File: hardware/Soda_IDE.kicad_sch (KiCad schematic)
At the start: 25 parts, among them CN1 MSX_SLOT_CON, J2 Conn_CF_Card, J3 Conn_02x22_Odd_Even, Q1 BC548, SW1 SW_Push, SW2 SW_Push_SPDT, U1 27C512, U2 74HCT74, U3 74LS32, U4 74HCT138

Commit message: fixes and updates
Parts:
- added JP2, JP3, JP4: SolderJumper_2_Open, Jumper:SolderJumper-2_P1.3mm_Open_RoundedPad1.0x1.5mm, symbol Jumper:SolderJumper_2_Open
- U2: renamed from U3; value 74LS32 -> 74HCT32
- renumbered C3 to C2, C2 to C3, D2 to D1, J3 to J1, JP2 to J2, J2 to J3, D1 to LD1, R6 to R1, R4 to R2, R5 to R3, R2 to R4, R1 to R5, R3 to R6, U2 to U3
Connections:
- net IORQ is gone; now on net ~{IORQ}: U3.13 (~{R})
- net ~{SEL} is gone; now on net ~{IDE_CS0}: J3.7 (Pin_7)
- net ~{IDE_CS0}: now also JP2.2 (B), JP3.2 (B), JP4.2 (B); no longer U4.13 (~{Y2})
- net at U4.12 (~{Y3}): now also JP2.1 (A)
- net at U4.15 (~{Y0}): now also JP4.1 (A)
- new net: JP3.1 (A), U4.13 (~{Y2})
- no-connect marks 62 -> 58
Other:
- note added: "JP2: 38h..3fh"
- note added: "JP3: 30h..37h"
- note added: "JP4 10h..17h"
- note added: "Z80 Reset (Optional)"
- note removed: "0011 0XXX"
- note removed: "30h..37h"
- moved on the sheet: C2, C3, CN1, SW2, U3B, U4

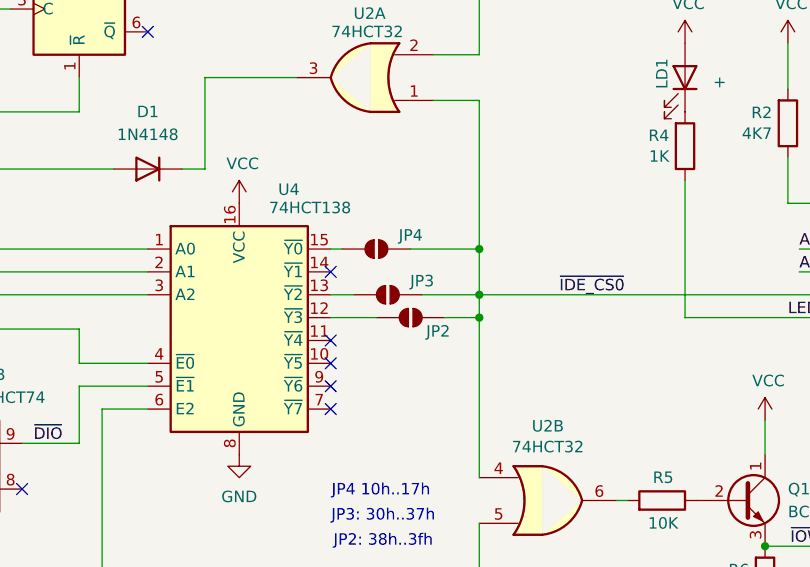
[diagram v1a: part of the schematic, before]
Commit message: conventional jumpers for address selection
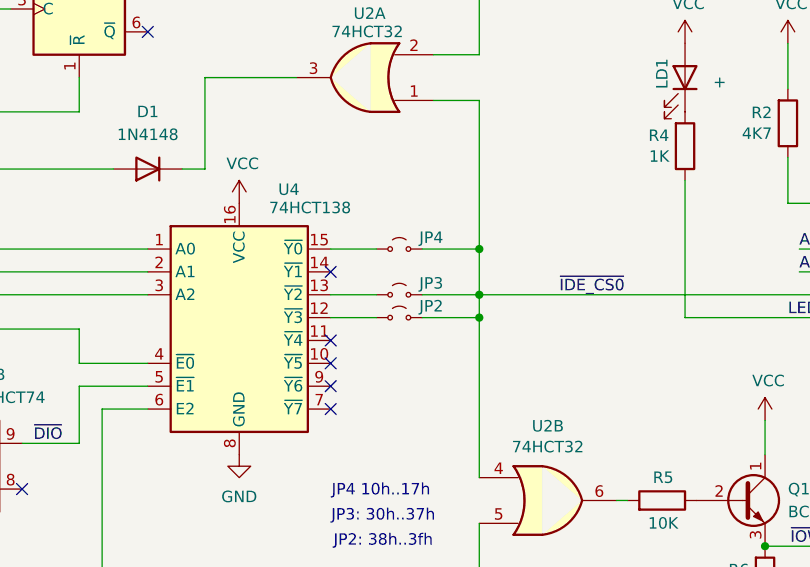
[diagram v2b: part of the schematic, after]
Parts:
- removed JP2, JP3, JP4: SolderJumper_2_Open, Jumper:SolderJumper-2_P1.3mm_Open_RoundedPad1.0x1.5mm, symbol Jumper:SolderJumper_2_Open
- added JP2, JP3, JP4: Jumper_2_Small_Open, Connector_PinHeader_2.54mm:PinHeader_1x02_P2.54mm_Vertical, symbol Jumper:Jumper_2_Small_Open
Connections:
- net ~{IDE_CS0}: now also JP2.2 (B), JP3.2 (B), JP4.2 (B)
- net at U4.15 (~{Y0}): now also JP4.1 (A)
- net at U4.12 (~{Y3}): now also JP2.1 (A)
- net at U4.13 (~{Y2}): now also JP3.1 (A)

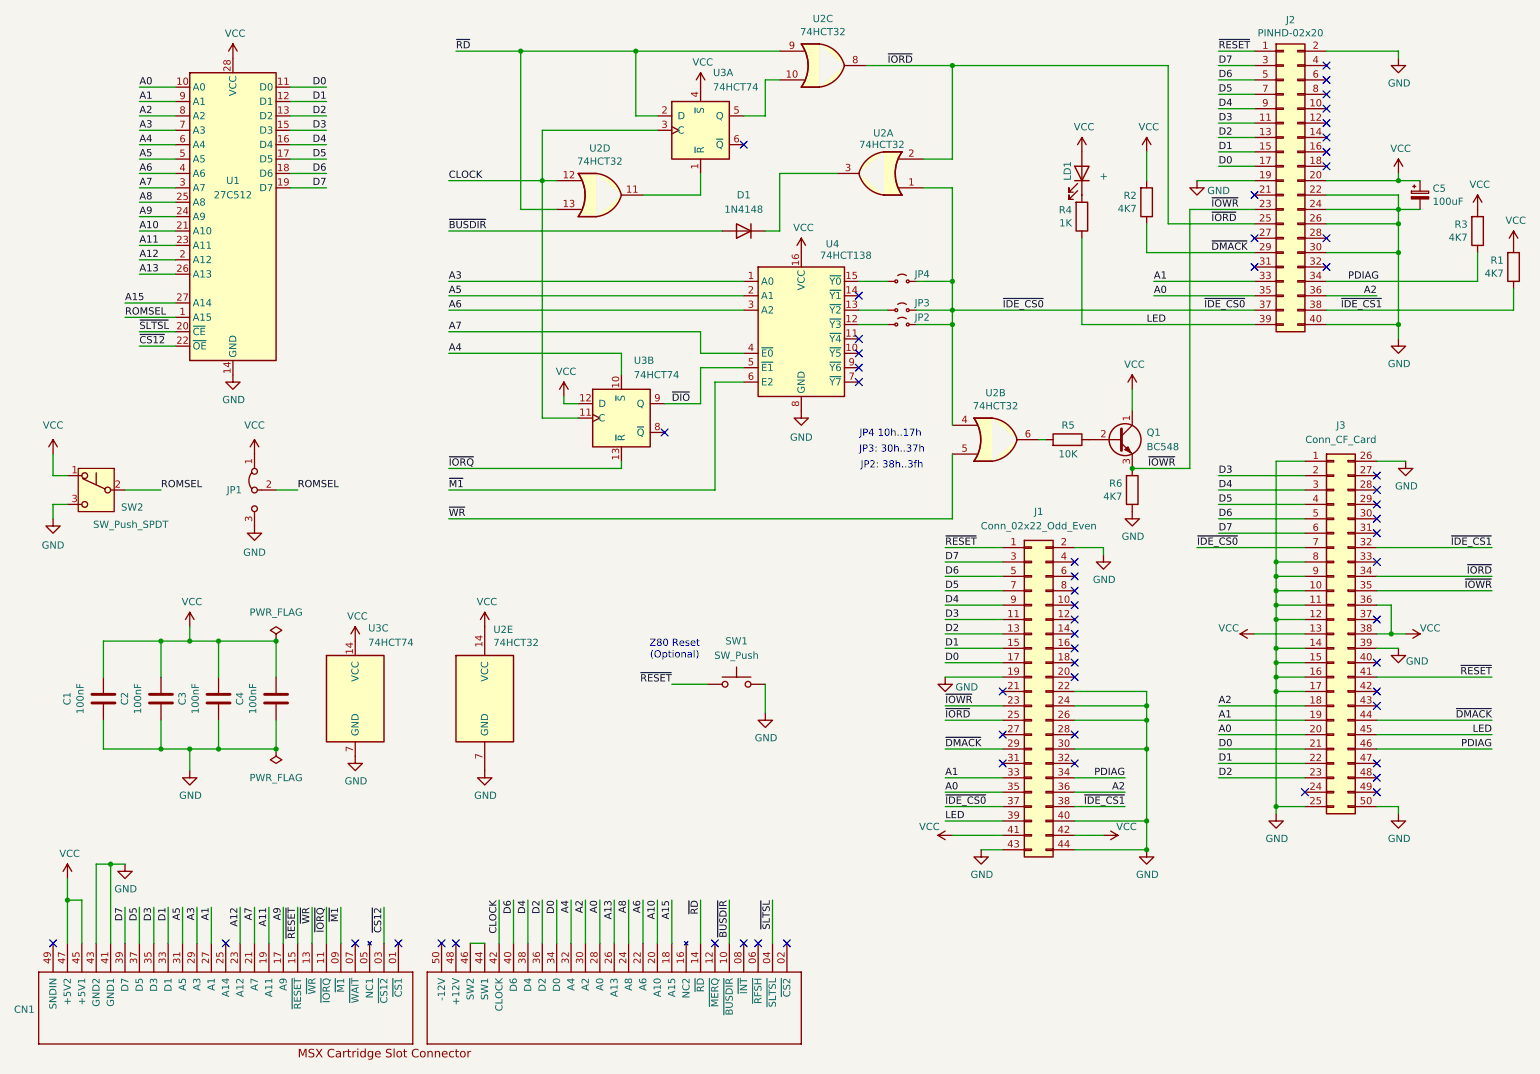
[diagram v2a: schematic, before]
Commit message: Added buffer to data lines
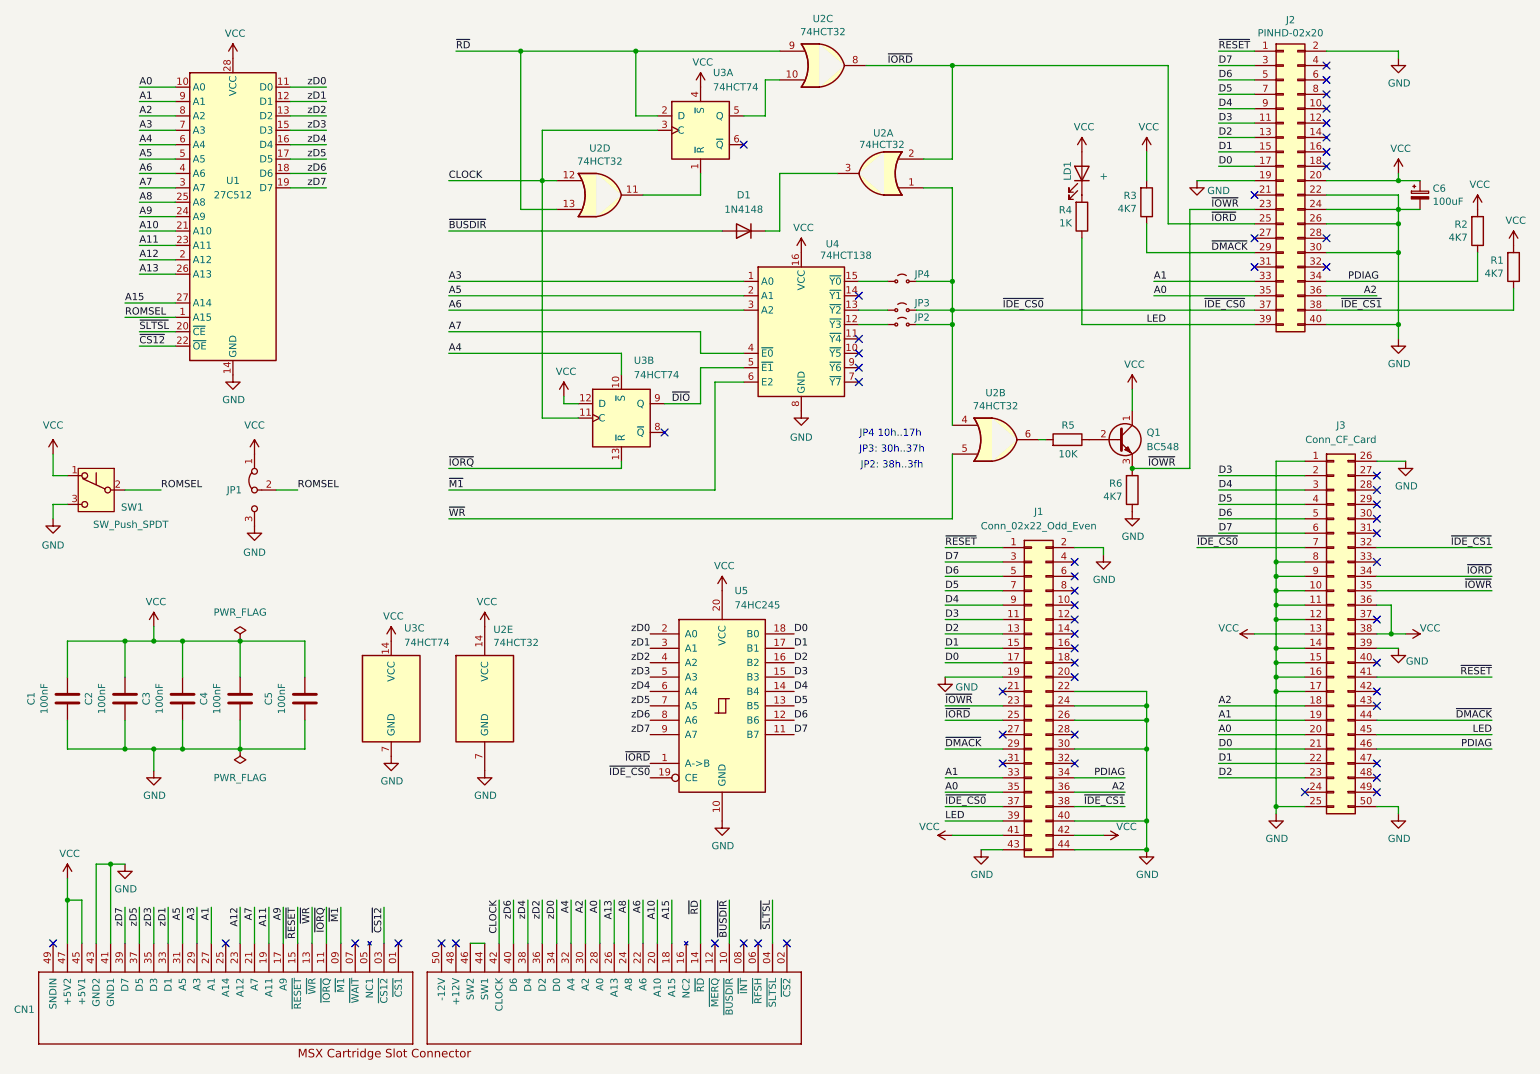
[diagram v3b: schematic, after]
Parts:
- removed SW1: SW_Push, Button_Switch_THT:SW_SPST_Omron_B3F-315x_Angled, symbol Switch:SW_Push
- added C5: 100nF, Capacitor_THT:C_Disc_D4.7mm_W2.5mm_P5.00mm, symbol Device:C
- added U5: 74HC245, Package_DIP:DIP-20_W7.62mm, symbol 74xx:74HC245
- renumbered C5 to C6, R3 to R2, R2 to R3, SW2 to SW1
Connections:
- net D0: now also U5.18 (B0); no longer CN1.34 (D0), U1.11 (D0)
- net D1: now also U5.17 (B1); no longer CN1.33 (D1), U1.12 (D1)
- net D2: now also U5.16 (B2); no longer CN1.36 (D2), U1.13 (D2)
- net D3: now also U5.15 (B3); no longer CN1.35 (D3), U1.15 (D3)
- net D4: now also U5.14 (B4); no longer CN1.38 (D4), U1.16 (D4)
- net D5: now also U5.13 (B5); no longer CN1.37 (D5), U1.17 (D5)
- net D6: now also U5.12 (B6); no longer CN1.40 (D6), U1.18 (D6)
- net D7: now also U5.11 (B7); no longer CN1.39 (D7), U1.19 (D7)
- net GND: now also C5.2, U5.10 (GND)
- net VCC: now also C5.1, U5.20 (VCC)
- net ~{IDE_CS0}: now also U5.19 (CE)
- net ~{IORD}: now also U5.1 (A->B)
- new net zD0: CN1.34 (D0), U1.11 (D0), U5.2 (A0)
- new net zD1: CN1.33 (D1), U1.12 (D1), U5.3 (A1)
- new net zD2: CN1.36 (D2), U1.13 (D2), U5.4 (A2)
- new net zD3: CN1.35 (D3), U1.15 (D3), U5.5 (A3)
- new net zD4: CN1.38 (D4), U1.16 (D4), U5.6 (A4)
- new net zD5: CN1.37 (D5), U1.17 (D5), U5.7 (A5)
- new net zD6: CN1.40 (D6), U1.18 (D6), U5.8 (A6)
- new net zD7: CN1.39 (D7), U1.19 (D7), U5.9 (A7)
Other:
- note removed: "Z80 Reset (Optional)"
- moved on the sheet: C1, C2, C3, C4, U3C

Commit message: updated board
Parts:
- renumbered R3 to R1, R1 to R3
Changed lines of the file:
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@@
 	(title_block
 		(title "Soda IDE")
-		(rev "v0.95")
+		(rev "v0.97")
 		(company "Danjovic 2024")
 		(comment 1 "Based on SC729 RCBus Compact Flash Modue v1.1.0 and Beer IDE 232")
@@
 		(on_board yes)
 		(dnp no)
-		(property "Reference" "R3"
+		(property "Reference" "R1"
 			(at 215.4174 44.5516 0)
 			(effects
@@
 			(project "SodaIDE"
 				(path "/fd20f746-7f7f-45d1-a0ab-bd0152a7988d"
-					(reference "R3")
+					(reference "R1")
 					(unit 1)
 				)
@@
 		(on_board yes)
 		(dnp no)
-		(property "Reference" "R1"
+		(property "Reference" "R3"
 			(at 280.1874 55.9816 0)
 			(effects
@@
 			(project "SodaIDE"
 				(path "/fd20f746-7f7f-45d1-a0ab-bd0152a7988d"
-					(reference "R1")
+					(reference "R3")
 					(unit 1)
 				)
